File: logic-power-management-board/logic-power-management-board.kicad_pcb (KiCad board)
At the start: 2 copper layers, 60 x 70 mm, 66 parts, among them IC1 MCP2562, J1 Conn_01x02, J2 Conn_01x02, J3 Conn_01x02, J4 Conn_01x02, J5 Conn_01x02, J6 Conn_01x04_Pin, J7 Conn_01x04, J8 Conn_01x04, J9 Conn_01x04, Q1 RS6L120BGTB1, Q2 RS6L120BGTB1, Q3 RS6L120BGTB1, SW1 SW_Push, SW2 SW_SPDT_312, U1 LM5050-1, U2 LM5050-1, U3 LM5050-1, U4 NJM12888F33, U5 STM32G431K8Tx

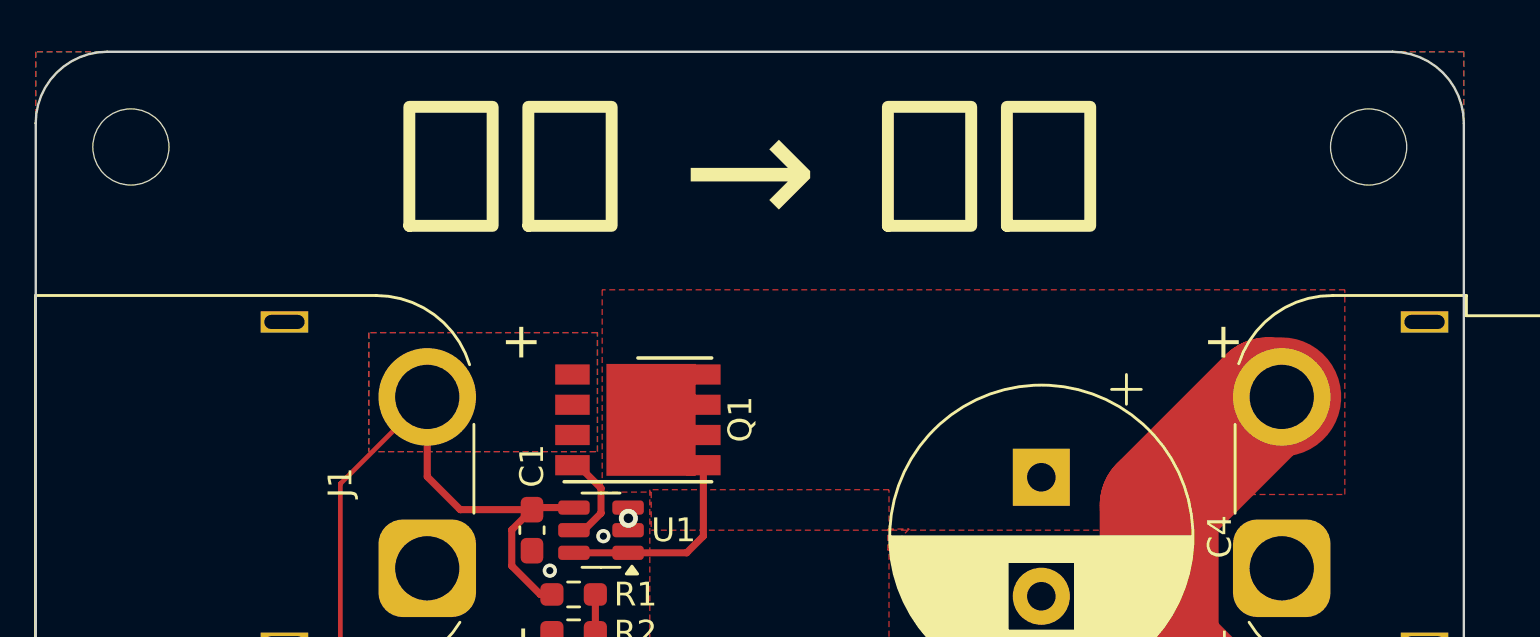
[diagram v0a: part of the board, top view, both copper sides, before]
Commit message: コンデンサー追加、シルク修正
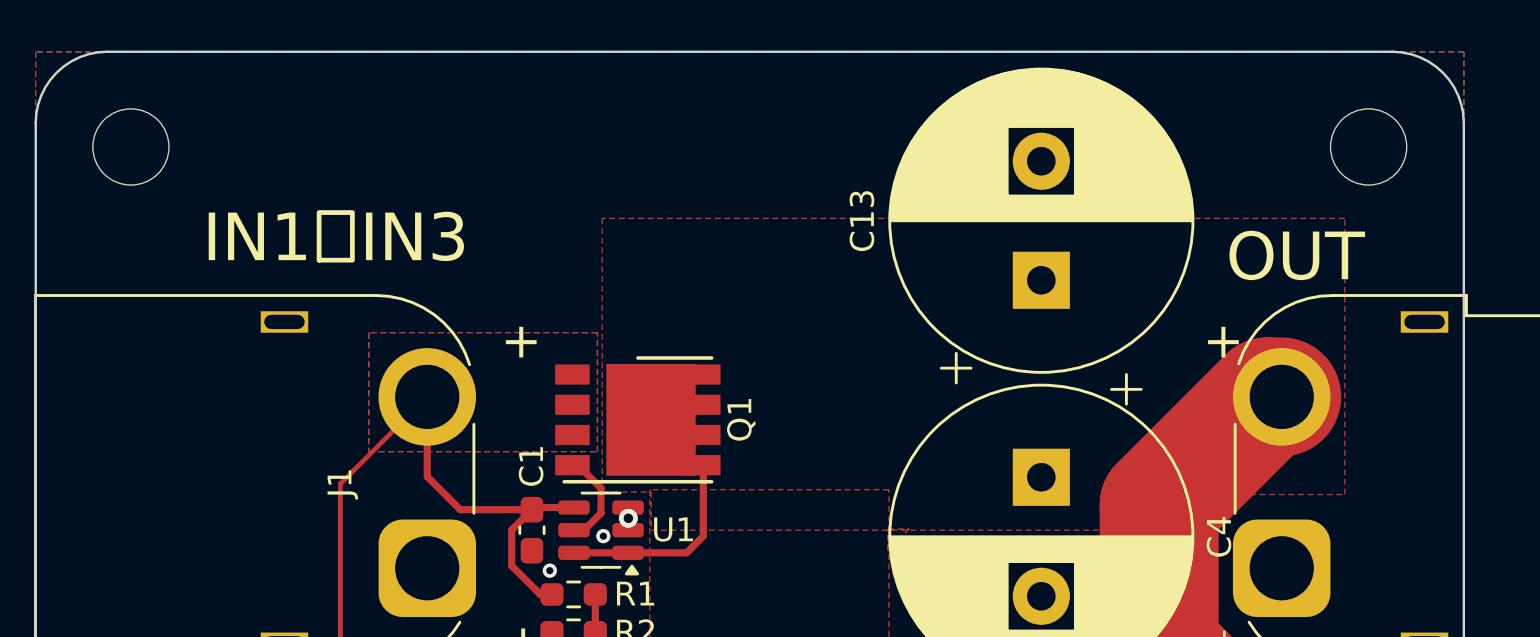
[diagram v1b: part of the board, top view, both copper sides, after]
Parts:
- added C13: 1000μF35V, Capacitor_THT:CP_Radial_D12.5mm_P5.00mm, F.Cu at (57.2, 24.6)
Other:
- board text added: "IN1〜IN3"
- board text added: "OUT"
- board text removed: "入力 → 出力"

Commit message: ガーバ生成
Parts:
- added G***: LOGO, LOGO, F.Cu at (43.6, 22.8)
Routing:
- net IN3: vias 5 -> 19
- net IN2: vias 2 -> 19
- net IN1: vias 0 -> 17
- net GNDD: vias 26 -> 333
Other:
- board text added: "logic-power-management-board version 1.0 create by ikeda"

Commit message: 配線、ビアの修正
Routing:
- net GNDD: vias 333 -> 339
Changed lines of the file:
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@@
 	)
 	(via
-		(at 47.2 76.6)
+		(at 47.15 76.2)
 		(size 0.6)
 		(drill 0.3)
@@
 	)
 	(via
-		(at 49.333297 74.3)
+		(at 49.375 74.325)
 		(size 0.6)
 		(drill 0.3)
@@
 	)
 	(via
+		(at 60.81318 77.99677)
+		(size 0.8)
+		(drill 0.4)
+		(layers "F.Cu" "B.Cu")
+		(free yes)
+		(net 1)
+	)
+	(via
 		(at 29 34)
 		(size 0.8)
@@
 	)
 	(via
-		(at 48.025 68.023528)
+		(at 48.025 68.023527)
 		(size 0.6)
 		(drill 0.3)
@@
 	)
 	(via
-		(at 48.2 70.6)
+		(at 48.2 71.3)
 		(size 0.6)
 		(drill 0.3)
@@
 	)
 	(via
+		(at 62.4 77.987499)
+		(size 0.8)
+		(drill 0.4)
+		(layers "F.Cu" "B.Cu")
+		(free yes)
+		(net 1)
+	)
+	(via
 		(at 72.5 50)
 		(size 0.8)
@@
 	)
 	(via
+		(at 51.65 79.075)
+		(size 0.8)
+		(drill 0.4)
+		(layers "F.Cu" "B.Cu")
+		(free yes)
+		(net 1)
+	)
+	(via
 		(at 22.5 25)
 		(size 0.8)
@@
 	)
 	(via
+		(at 58.125 76.4)
+		(size 0.8)
+		(drill 0.4)
+		(layers "F.Cu" "B.Cu")
+		(free yes)
+		(net 1)
+	)
+	(via
 		(at 20 57.5)
 		(size 0.8)
@@
 	)
 	(via
+		(at 61.2 81.6)
+		(size 0.8)
+		(drill 0.4)
+		(layers "F.Cu" "B.Cu")
+		(free yes)
+		(net 1)
+	)
+	(via
 		(at 17.5 47.5)
 		(size 0.8)
@@
 	)
 	(via
+		(at 53.8 77.925)
+		(size 0.8)
+		(drill 0.4)
+		(layers "F.Cu" "B.Cu")
+		(free yes)
+		(net 1)
+	)
+	(via
 		(at 57 84)
 		(size 0.8)
@@
 	)
 	(segment
-		(start 47.25 72.15)
-		(end 47.25 72.75)
-		(width 0.2)
-		(layer "F.Cu")
-		(net 7)
-	)
-	(segment
 		(start 45.6 72.8625)
 		(end 47.1375 72.8625)
@@
 	)
 	(segment
+		(start 48.64 73.83)
+		(end 49.15 73.32)
+		(width 0.2)
+		(layer "F.Cu")
+		(net 7)
+	)
+	(segment
 		(start 59.82 80.165)
 		(end 61.9725 80.165)
@@
 	)
 	(segment
+		(start 47.655 73.83)
+		(end 48.64 73.83)
+		(width 0.2)
+		(layer "F.Cu")
+		(net 7)
+	)
+	(segment
 		(start 64.8125 78.075)
 		(end 65.6 77.2875)
@@
 	)
 	(segment
-		(start 47.8 71.6)
-		(end 47.25 72.15)
+		(start 49.15 73.32)
+		(end 49.15 72.75)
 		(width 0.2)
 		(layer "F.Cu")
@@
 	)
 	(segment
-		(start 49.15 72.15)
-		(end 48.6 71.6)
+		(start 47.25 72.75)
+		(end 47.25 73.425)
 		(width 0.2)
 		(layer "F.Cu")
@@
 	)
 	(segment
-		(start 48.6 71.6)
-		(end 47.8 71.6)
+		(start 47.25 73.425)
+		(end 47.655 73.83)
 		(width 0.2)
 		(layer "F.Cu")
@@
 		(net 7)
 	)
-	(segment
-		(start 49.15 72.75)
-		(end 49.15 72.15)
-		(width 0.2)
-		(layer "F.Cu")
-		(net 7)
-	)
 	(via
 		(at 57.6 72.2)
@@
 	)
 	(zone
+		(net 0)
+		(net_name "")
+		(layer "F.Cu")
+		(hatch edge 0.5)
+		(connect_pads
+			(clearance 0)
+		)
+		(min_thickness 0.25)
+		(filled_areas_thickness no)
+		(keepout
+			(tracks allowed)
+			(vias allowed)
+			(pads allowed)
+			(copperpour not_allowed)
+			(footprints allowed)
+		)
+		(fill
+			(thermal_gap 0.5)
+			(thermal_bridge_width 0.5)
+		)
+		(polygon
+			(pts
+				(xy 57.6 76.2) (xy 57.6 77.2) (xy 56.6 76.8)
+			)
+		)
+	)
+	(zone
 		(net 8)
 		(net_name "OUT")
@@
 	)
 	(zone
+		(net 0)
+		(net_name "")
+		(layer "F.Cu")
+		(hatch edge 0.5)
+		(connect_pads
+			(clearance 0)
+		)
+		(min_thickness 0.25)
+		(filled_areas_thickness no)
+		(keepout
+			(tracks allowed)
+			(vias allowed)
+			(pads allowed)
+			(copperpour not_allowed)
+			(footprints allowed)
+		)
+		(fill
+			(thermal_gap 0.5)
+			(thermal_bridge_width 0.5)
+		)
+		(polygon
+			(pts
+				(xy 56 80.2) (xy 56 81.2) (xy 55 80.8)
+			)
+		)
+	)
+	(zone
 		(net 8)
 		(net_name "OUT")
@@
 			)
 		)
+	)
+	(zone
+		(net 0)
+		(net_name "")
+		(layers "F.Cu" "B.Cu")
+		(hatch edge 0.5)
+		(connect_pads
+			(clearance 0)
+		)
+		(min_thickness 0.25)
+		(filled_areas_thickness no)
+		(keepout
+			(tracks allowed)
+			(vias allowed)
+			(pads allowed)
+			(copperpour not_allowed)
+			(footprints allowed)
+		)
+		(fill
+			(thermal_gap 0.5)
+			(thermal_bridge_width 0.5)
+		)
+		(polygon
+			(pts
+				(xy 46.875 75.5) (xy 47.325 75.5) (xy 47.325 74.825)
+			)
+		)
